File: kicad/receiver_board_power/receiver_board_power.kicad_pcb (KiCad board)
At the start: 2 copper layers, 31 x 47.5 mm, 7 parts, among them J1 Battery Conn, J2 B2B, SW1 On/Off, U1 2S BMS, U2 5V Buck

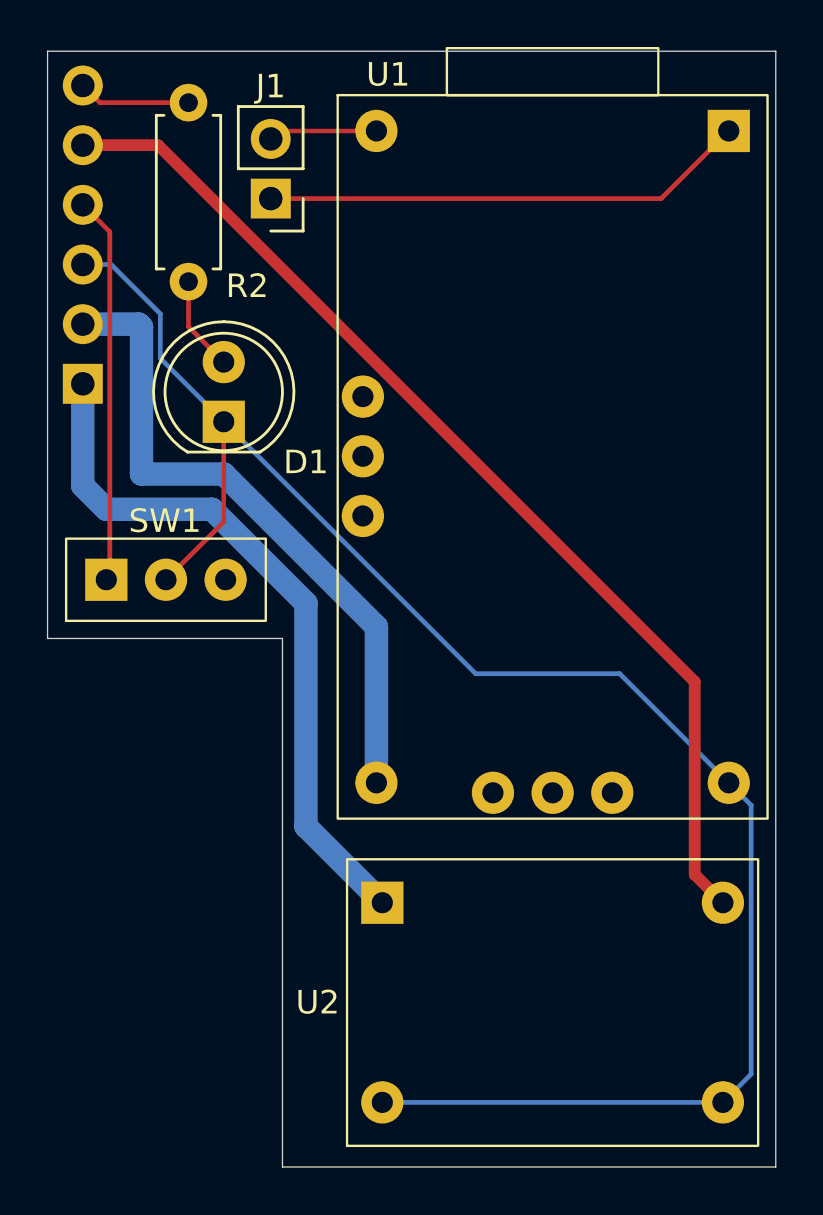
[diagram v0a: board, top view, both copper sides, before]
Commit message: Add battery monitor connector and update receiver power board layout
- Add 3-pin battery monitor connector (J3) to receiver power board
  - Connected to BMS balance leads (B+, BM, B-)
  - Enables individual cell voltage monitoring
- Update receiver power board PCB layout and routing
- Export updated netlists for all three boards
- Add BMS reference image (bom/images/2S_BMS.jpg)
- Add *.lck to .gitignore to exclude KiCad lock files

Co-Authored-By: Claude Sonnet 4.5 <noreply@anthropic.com>
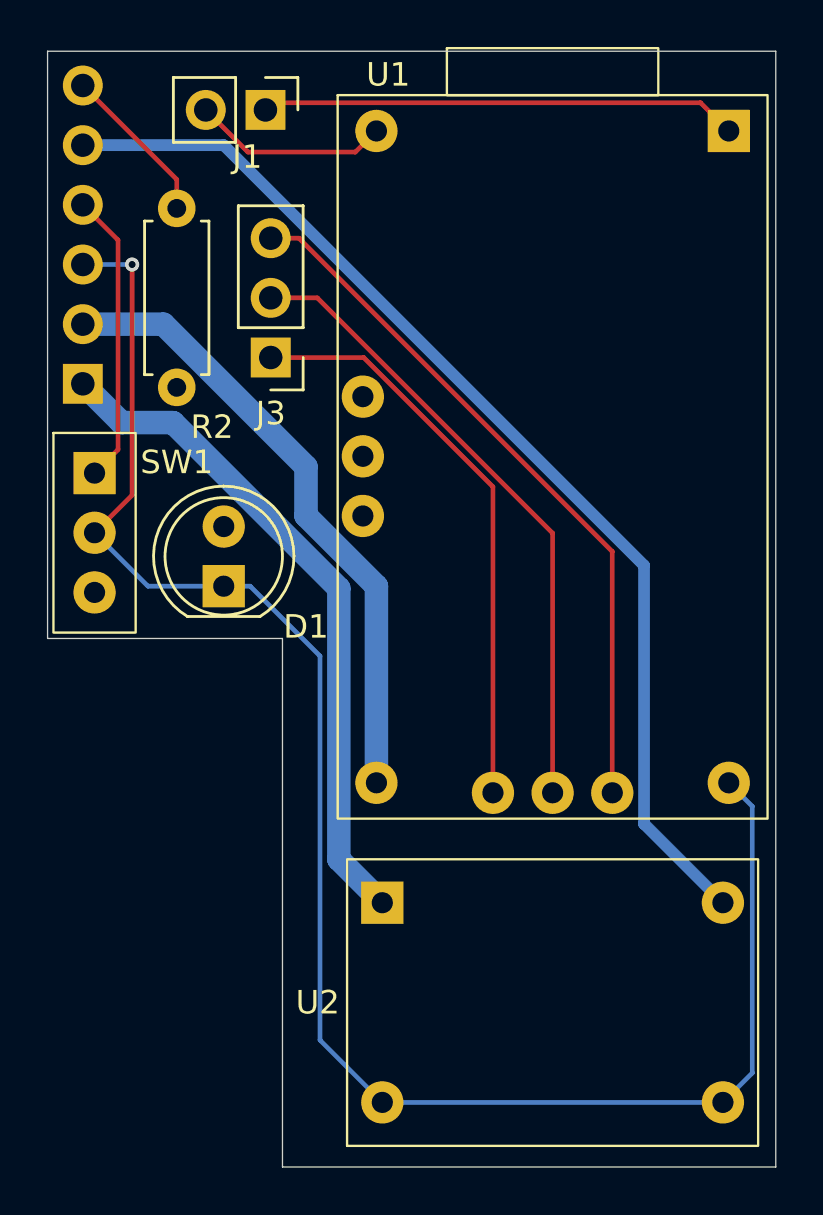
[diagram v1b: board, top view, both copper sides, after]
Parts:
- added J3: Battery Mon, Connector_PinHeader_2.54mm:PinHeader_1x03_P2.54mm_Vertical, F.Cu at (109.5, 63.0)
- moved D1 7.00 mm to (107.5, 72.8)
- moved R2 4.53 mm to (105.5, 64.3)
- moved J1 3.78 mm to (109.3, 52.5), turned to -90 degrees
- moved SW1 3.64 mm to (102.0, 70.5), turned to 0 degrees
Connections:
- U1 pad 7: unconnected-(U1-B+-Pad7) -> Net-(J3-Pin_1)
- U1 pad 8: unconnected-(U1-BM-Pad8) -> Net-(J3-Pin_2)
- U1 pad 9: unconnected-(U1-B--Pad9) -> Net-(J3-Pin_3)
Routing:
- net Net-(J3-Pin_3): track 0.00 -> 30.3 mm
- net Net-(J3-Pin_2): track 0.00 -> 27.2 mm
- net Net-(J3-Pin_1): track 0.00 -> 24.8 mm
- net Net-(D1-A): track 4.05 -> 0.00 mm
- net /PWR_SW: track 16.5 -> 12.5 mm
- net Net-(J1-Pin_2): track 5.12 -> 8.38 mm
- net /LED_ESP: track 4.80 -> 6.89 mm
- net /5v_BUCK: track 45.4 -> 47.1 mm
- net /7v4_FET: track 30.0 -> 28.7 mm
- net /7v4_BMS: track 28.1 -> 27.0 mm
- net /GND: track 75.4 -> 75.1 mm, vias 0 -> 1

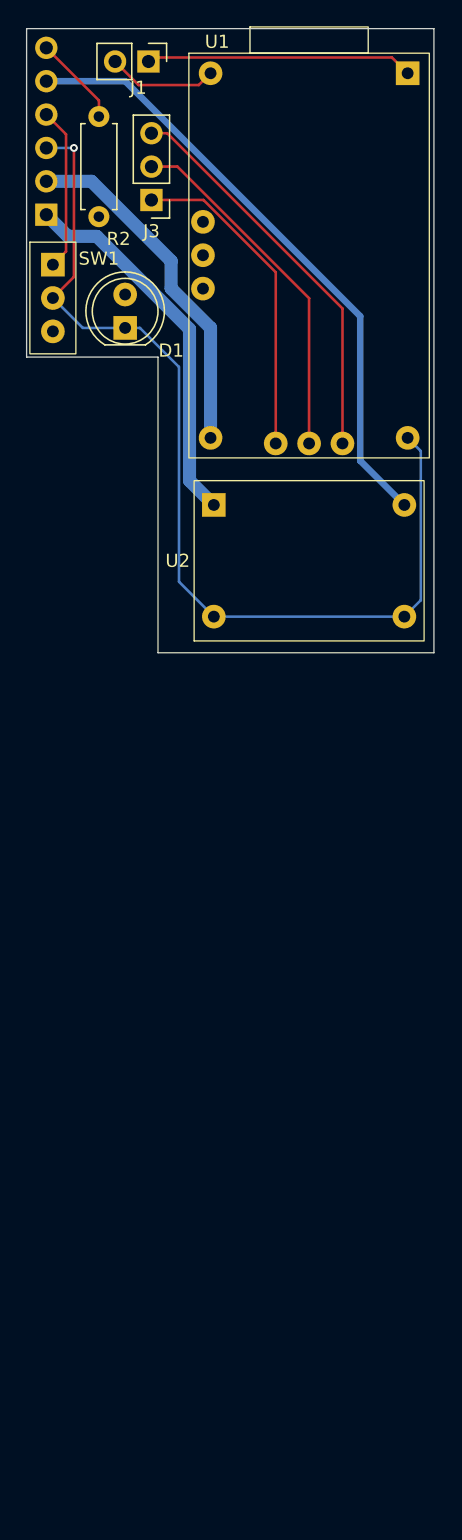
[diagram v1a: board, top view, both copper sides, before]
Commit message: Remove BMS and reorganize receiver boards for external charging
Major schematic and layout revision based on EE review:

- Remove BMS from receiver design; pivot to external LiPo charging
- Reorganize components between power and logic boards:
  - Logic board: P-FET power switch, buck converter, UI (LED/button), debug UART
  - Power board: ESP32-C3, motor driver, battery monitoring
- Add voltage dividers for 2S LiPo monitoring (B+ and BM)
  - Safe ADC voltages: B+ = 2.36V max, BM = 2.47V max
- Add debug UART headers (GPIO20/21) for serial output when USB unavailable
- Fix P-FET drain connection to properly power both buck and motor system
- Update B2B connectors to dual 6-pin configuration (signal + power)
- Minor controller board PCB layout adjustments

Co-Authored-By: Claude Sonnet 4.5 <noreply@anthropic.com>
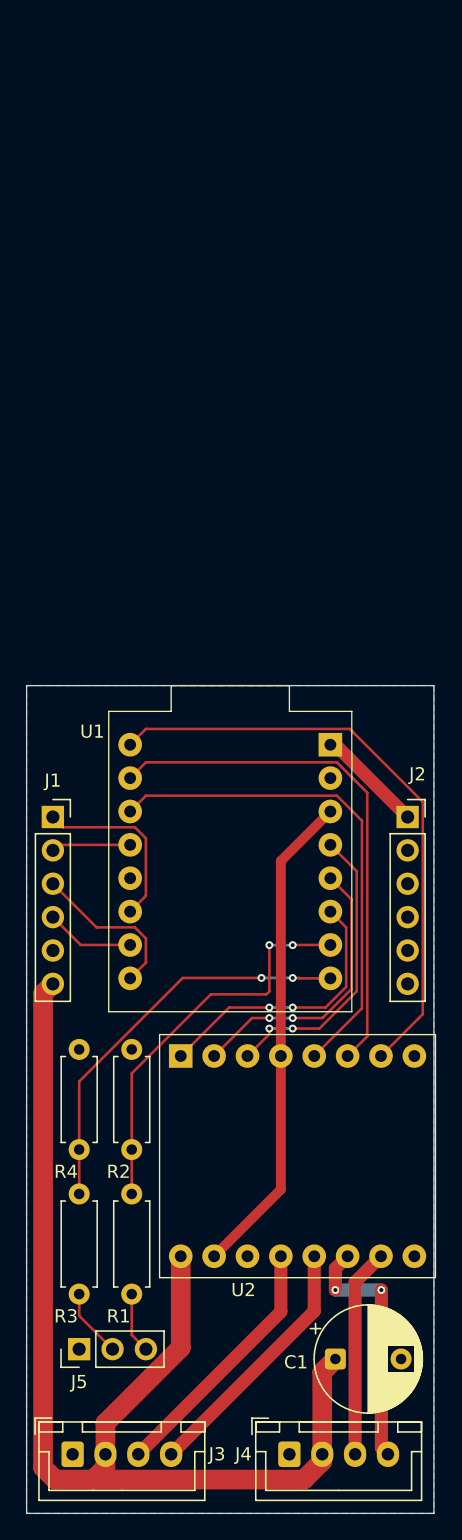
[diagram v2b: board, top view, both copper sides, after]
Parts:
- removed D1: Status, LED_THT:LED_D5.0mm
- removed SW1: On/Off, ESP32_Lego_PF:Slide_Switch_SPDT_12D00G
- added C1: 470uF, Capacitor_THT:CP_Radial_D8.0mm_P5.00mm, F.Cu at (123.5, 151.2)
- added J4: Motor 2, Connector_JST:JST_XH_B4B-XH-A_1x04_P2.50mm_Vertical, F.Cu at (120.0, 158.5)
- added J5: Battery Mon, Connector_PinHeader_2.54mm:PinHeader_1x03_P2.54mm_Vertical, F.Cu at (104.0, 150.5)
- added R1: 100k, Resistor_THT:R_Axial_DIN0207_L6.3mm_D2.5mm_P7.62mm_Horizontal, F.Cu at (108.0, 146.3)
- added R3: 33k, Resistor_THT:R_Axial_DIN0207_L6.3mm_D2.5mm_P7.62mm_Horizontal, F.Cu at (104.0, 146.3)
- added R4: 47k, Resistor_THT:R_Axial_DIN0207_L6.3mm_D2.5mm_P7.62mm_Horizontal, F.Cu at (104.0, 135.3)
- J1: value Battery Conn -> B2B 1; footprint Connector_PinHeader_2.54mm:PinHeader_1x02_P2.54mm_Vertical -> Connector_PinSocket_2.54mm:PinSocket_1x06_P2.54mm_Vertical
- J2: value B2B -> B2B 2; footprint Connector_PinHeader_2.54mm:PinHeader_1x06_P2.54mm_Vertical -> Connector_PinSocket_2.54mm:PinSocket_1x06_P2.54mm_Vertical; moved to F.Cu
- J3: value Battery Mon -> Motor 1; footprint Connector_PinHeader_2.54mm:PinHeader_1x03_P2.54mm_Vertical -> Connector_JST:JST_XH_B4B-XH-A_1x04_P2.50mm_Vertical
- R2: value 1k -> 39k
- U1: value 2S BMS -> ESP32-C3-SuperMini; footprint ESP32_Lego_PF:2S BMS -> ESP32_Lego_PF:ESP32-C3-SuperMini
- U2: value 5V Buck -> Dual H Bridge; footprint ESP32_Lego_PF:MP1584EN -> ESP32_Lego_PF:TB6612FNG
- moved J3 95.6 mm to (103.5, 158.5), turned to 0 degrees
- moved R2 71.0 mm to (108.0, 135.3)
- moved J1 58.0 mm to (102.0, 110.0), turned to 0 degrees
- moved J2 53.5 mm to (129.0, 110.0)
- moved U2 45.3 mm to (120.6, 135.8)
- moved U1 37.7 mm to (115.5, 104.5)
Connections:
- J1 pad 1: Net-(J1-Pin_1) -> /BUT_ESP
- J1 pad 2: Net-(J1-Pin_2) -> /LED_ESP
- J2 pad 1: /7v4_FET -> /5v_BUCK
- J2 pad 2: /7v4_BMS -> /GND
- J2 pad 4: /PWR_SW -> /GND
- J2 pad 5: /5v_BUCK -> /GND
- J2 pad 6: /LED_ESP -> /GND
- J3 pad 1: Net-(J3-Pin_1) -> /GND
- J3 pad 2: Net-(J3-Pin_2) -> /7v4_FET
- J3 pad 3: Net-(J3-Pin_3) -> /MOT1_C1
- R2 pad 1: Net-(D1-A) -> /B+_DIV
- R2 pad 2: /LED_ESP -> /GND
- U1 pad 1: Net-(J1-Pin_1) -> /5v_BUCK
- U1 pad 10: /GND -> /RX
- U1 pad 2: Net-(J1-Pin_2) -> /GND
- U1 pad 3: unconnected-(U1-LED-Pad3) -> /3v3_ESP
- U1 pad 4: unconnected-(U1-NTC-Pad4) -> /MOT1_IN1
- U1 pad 5: unconnected-(U1-GND-Pad5) -> /MOT1_IN2
- U1 pad 6: /7v4_BMS -> /MOT1_PWM
- U1 pad 7: Net-(J3-Pin_1) -> /B+_DIV
- U1 pad 8: Net-(J3-Pin_2) -> /BM_DIV
- U1 pad 9: Net-(J3-Pin_3) -> /TX
- U2 pad 1: /7v4_FET -> /MOT1_PWM
- U2 pad 2: /GND -> /MOT1_IN2
- U2 pad 3: /GND -> /MOT1_IN1
- U2 pad 4: /5v_BUCK -> /3v3_ESP
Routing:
- net /GND: track 75.1 -> 0.00 mm, vias 1 -> 0
- net /7v4_FET: track 28.7 -> 87.3 mm
- net /MOT2_PWM: track 0.00 -> 45.7 mm
- net /MOT2_IN2: track 0.00 -> 40.2 mm
- net /5v_BUCK: track 47.1 -> 8.16 mm
- net /MOT2_IN1: track 0.00 -> 38.3 mm
- net /3v3_ESP: track 0.00 -> 37.5 mm
- net /BM_DIV: track 0.00 -> 31.0 mm, vias 0 -> 2
- net /B+_DIV: track 0.00 -> 30.4 mm, vias 0 -> 2
- net Net-(J3-Pin_3): track 30.3 -> 0.00 mm
- net Net-(J3-Pin_2): track 27.2 -> 0.00 mm
- net /7v4_BMS: track 27.0 -> 0.00 mm
- net Net-(J3-Pin_1): track 24.8 -> 0.00 mm
- net /MOT1_IN1: track 0.00 -> 22.6 mm, vias 0 -> 2
- net /MOT1_IN2: track 0.00 -> 21.7 mm, vias 0 -> 2
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- added copper zone on B.Cu, net /GND
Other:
- board size 31 x 47.5 mm -> 31 x 63 mm

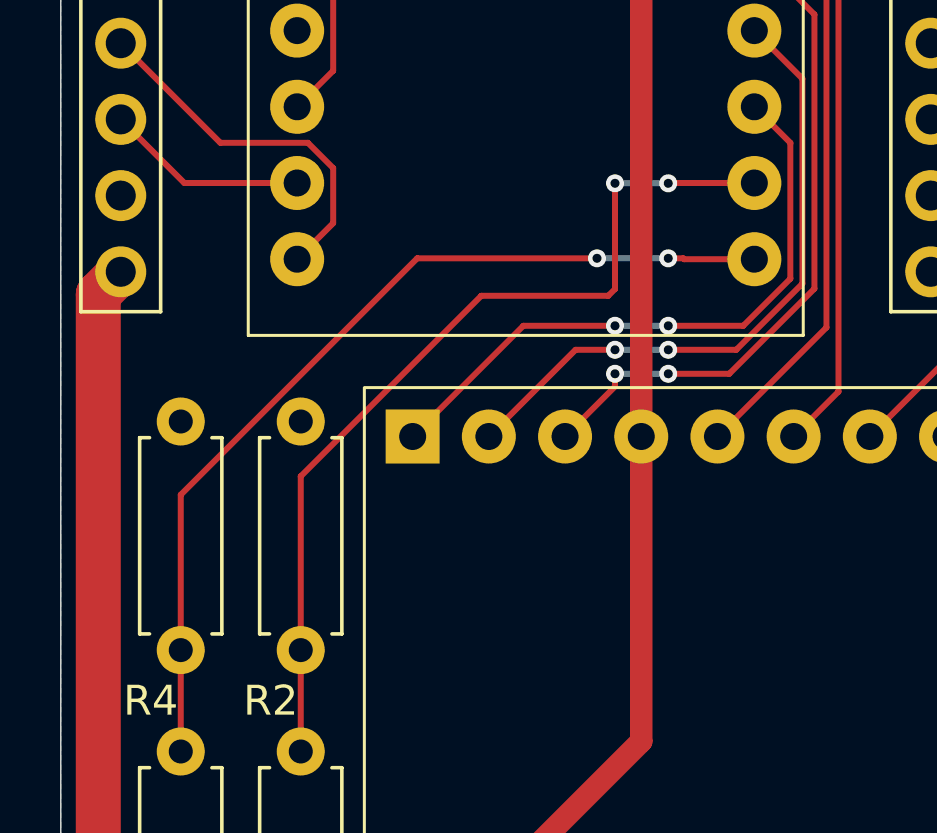
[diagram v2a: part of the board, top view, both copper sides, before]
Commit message: Add battery monitoring module with unit tests and swap B+/BM GPIOs
Add lib/battery.py for 2S LiPo voltage monitoring via hardware voltage
dividers (B+ on GPIO0, BM on GPIO1). Includes per-cell voltage tracking,
status detection (OK/LOW/CRITICAL/IMBALANCED), and percentage estimation.

Add tests/test_battery.py with 25 unit tests covering voltage conversion,
status thresholds, percentage clamping, cell imbalance, and edge cases.

Update deploy scripts, documentation, and KiCad schematic/PCB to swap
B+ and BM GPIO assignments for cleaner PCB routing.

Co-Authored-By: Claude Opus 4.5 <noreply@anthropic.com>
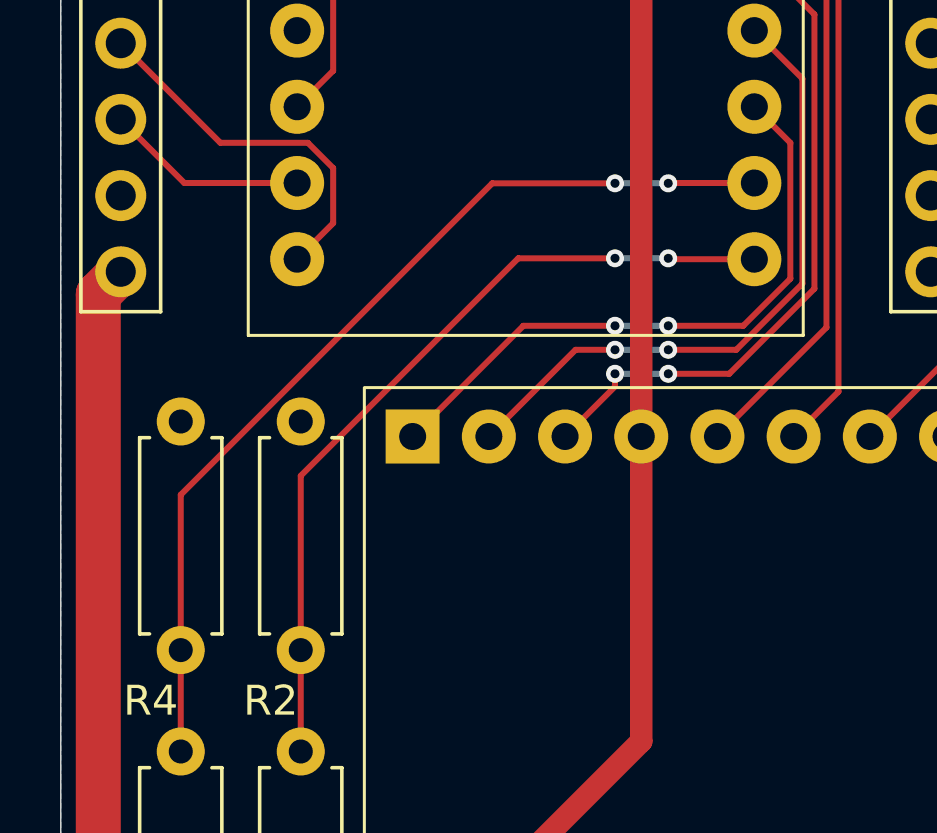
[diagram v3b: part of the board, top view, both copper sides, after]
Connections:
- U1 pad 7: /B+_DIV -> /BM_DIV
- U1 pad 8: /BM_DIV -> /B+_DIV
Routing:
- net /B+_DIV: track 30.4 -> 27.3 mm
- net /BM_DIV: track 31.0 -> 32.0 mm
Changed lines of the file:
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@@
 			(layers "*.Cu" "*.Mask")
 			(remove_unused_layers no)
-			(net 19 "/B+_DIV")
+			(net 20 "/BM_DIV")
 			(pinfunction "IO1")
 			(pintype "bidirectional")
@@
 			(layers "*.Cu" "*.Mask")
 			(remove_unused_layers no)
-			(net 20 "/BM_DIV")
+			(net 19 "/B+_DIV")
 			(pinfunction "IO0")
 			(pintype "bidirectional")
@@
 	)
 	(segment
-		(start 108 135.31)
-		(end 108 129.518)
+		(start 118.475 122.25)
+		(end 115.25 122.25)
 		(width 0.2)
 		(layer "F.Cu")
@@
 	)
 	(segment
-		(start 118.475 123.275)
-		(end 118.475 119.75)
-		(width 0.2)
-		(layer "F.Cu")
-		(net 19)
-	)
-	(segment
-		(start 114.018 123.5)
-		(end 118.25 123.5)
-		(width 0.2)
-		(layer "F.Cu")
-		(net 19)
-	)
-	(segment
-		(start 120.25 119.75)
-		(end 120.26 119.74)
+		(start 115.25 122.25)
+		(end 108 129.5)
 		(width 0.2)
 		(layer "F.Cu")
@@
 	)
 	(segment
+		(start 120.28 122.28)
+		(end 120.25 122.25)
+		(width 0.2)
+		(layer "F.Cu")
+		(net 19)
+	)
+	(segment
+		(start 108 129.5)
+		(end 108 135.31)
+		(width 0.2)
+		(layer "F.Cu")
+		(net 19)
+	)
+	(segment
+		(start 123.12 122.28)
+		(end 120.28 122.28)
+		(width 0.2)
+		(layer "F.Cu")
+		(net 19)
+	)
+	(via
+		(at 118.475 122.25)
+		(size 0.6)
+		(drill 0.3)
+		(layers "F.Cu" "B.Cu")
+		(net 19)
+	)
+	(via
+		(at 120.25 122.25)
+		(size 0.6)
+		(drill 0.3)
+		(layers "F.Cu" "B.Cu")
+		(net 19)
+	)
+	(segment
+		(start 120.25 122.25)
+		(end 118.475 122.25)
+		(width 0.2)
+		(layer "B.Cu")
+		(net 19)
+	)
+	(segment
+		(start 104 130.13295)
+		(end 104 135.31)
+		(width 0.2)
+		(layer "F.Cu")
+		(net 20)
+	)
+	(segment
+		(start 118.475 119.75)
+		(end 114.38295 119.75)
+		(width 0.2)
+		(layer "F.Cu")
+		(net 20)
+	)
+	(segment
+		(start 114.38295 119.75)
+		(end 104 130.13295)
+		(width 0.2)
+		(layer "F.Cu")
+		(net 20)
+	)
+	(segment
 		(start 120.26 119.74)
-		(end 123.12 119.74)
-		(width 0.2)
-		(layer "F.Cu")
-		(net 19)
-	)
-	(segment
-		(start 118.25 123.5)
-		(end 118.475 123.275)
-		(width 0.2)
-		(layer "F.Cu")
-		(net 19)
-	)
-	(segment
-		(start 108 129.518)
-		(end 114.018 123.5)
-		(width 0.2)
-		(layer "F.Cu")
-		(net 19)
+		(end 120.25 119.75)
+		(width 0.2)
+		(layer "F.Cu")
+		(net 20)
+	)
+	(segment
+		(start 104 138.69)
+		(end 104 135.31)
+		(width 0.2)
+		(layer "F.Cu")
+		(net 20)
+	)
+	(segment
+		(start 123.12 119.74)
+		(end 120.26 119.74)
+		(width 0.2)
+		(layer "F.Cu")
+		(net 20)
+	)
+	(via
+		(at 120.25 119.75)
+		(size 0.6)
+		(drill 0.3)
+		(layers "F.Cu" "B.Cu")
+		(net 20)
 	)
 	(via
@@
 		(drill 0.3)
 		(layers "F.Cu" "B.Cu")
-		(net 19)
-	)
-	(via
-		(at 120.25 119.75)
-		(size 0.6)
-		(drill 0.3)
-		(layers "F.Cu" "B.Cu")
-		(net 19)
-	)
-	(segment
-		(start 118.475 119.75)
-		(end 120.25 119.75)
+		(net 20)
+	)
+	(segment
+		(start 120.25 119.75)
+		(end 118.475 119.75)
 		(width 0.2)
 		(layer "B.Cu")
-		(net 19)
-	)
-	(segment
-		(start 120.75 122.25)
-		(end 120.78 122.28)
-		(width 0.2)
-		(layer "F.Cu")
-		(net 20)
-	)
-	(segment
-		(start 111.88295 122.25)
-		(end 117.875 122.25)
-		(width 0.2)
-		(layer "F.Cu")
-		(net 20)
-	)
-	(segment
-		(start 104 138.69)
-		(end 104 135.31)
-		(width 0.2)
-		(layer "F.Cu")
-		(net 20)
-	)
-	(segment
-		(start 120.25 122.25)
-		(end 120.75 122.25)
-		(width 0.2)
-		(layer "F.Cu")
-		(net 20)
-	)
-	(segment
-		(start 104 135.31)
-		(end 104 130.13295)
-		(width 0.2)
-		(layer "F.Cu")
-		(net 20)
-	)
-	(segment
-		(start 120.78 122.28)
-		(end 123.12 122.28)
-		(width 0.2)
-		(layer "F.Cu")
-		(net 20)
-	)
-	(segment
-		(start 104 130.13295)
-		(end 111.88295 122.25)
-		(width 0.2)
-		(layer "F.Cu")
-		(net 20)
-	)
-	(via
-		(at 117.875 122.25)
-		(size 0.6)
-		(drill 0.3)
-		(layers "F.Cu" "B.Cu")
-		(net 20)
-	)
-	(via
-		(at 120.25 122.25)
-		(size 0.6)
-		(drill 0.3)
-		(layers "F.Cu" "B.Cu")
-		(net 20)
-	)
-	(segment
-		(start 117.875 122.25)
-		(end 120.25 122.25)
-		(width 0.2)
-		(layer "B.Cu")
